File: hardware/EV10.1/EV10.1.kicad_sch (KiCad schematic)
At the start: 105 parts, among them J1 Conn_01x02_Socket, J10 Conn_01x08_Socket, J11 Conn_01x06_Female, J13 Conn_01x04_Female, J2 Conn_01x02_Female, J5 Conn_01x02_Socket, J7 Conn_01x04_Female, J8 Conn_01x06_Female, J9 USB_C_Receptacle, SW4 SW_Push, SW5 SW_Push, U1 STM32F405RGTx, U11 ESP32-S3-WROOM-1-N8R2, U13 BM14B(0.8)-24DS-0.4V(53), U2 BQ21040DBVR, U3 CH340C, U4 USBLC6-2P6, U5 STM32F030C8Tx, U6 WM8960CGEFL/RV, U7 TPS63060, Y1 Crystal_GND24

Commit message: Fix most warnings and errors in EV10.1
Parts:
- removed J9: USB_C_Receptacle, Connector_USB:USB_C_Receptacle_HRO_TYPE-C-31-M-12, symbol Connector:USB_C_Receptacle
- removed R2, R3: 5k1, Resistor_SMD:R_0402_1005Metric, symbol Device:R
- added R28, R29: 5k1, Resistor_SMD:R_0402_1005Metric, symbol Device:R
- added USB_C1: TYPE-C-31-M-12, Connector_USB:USB_C_Receptacle_HRO_TYPE-C-31-M-12, symbol jlcpcb:TYPE-C-31-M-12
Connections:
- net GND: now also U6.28 (AGND), R28.1, R29.1, USB_C1.0 (SH), USB_C1.A1 (GND), USB_C1.A12 (GND), USB_C1.B1 (GND), USB_C1.B12 (GND)
- net I2S_ADCDAT: now also U1.56 (PB4); no longer U1.52 (PC11)
- net I2S_DACDAT: now also U1.57 (PB5); no longer U1.53 (PC12)
- net KB_COL5: now also U1.53 (PC12); no longer U1.57 (PB5)
- net KB_ROW7: now also U1.52 (PC11); no longer U1.56 (PB4)
- net USB_D+: now also USB_C1.A6 (DP1), USB_C1.B6 (DP2)
- net USB_D-: now also USB_C1.A7 (DN1), USB_C1.B7 (DN2)
- net VBUS: now also USB_C1.A4 (VBUS), USB_C1.A9 (VBUS), USB_C1.B4 (VBUS), USB_C1.B9 (VBUS)
- new net: R29.2, USB_C1.B5 (CC2)
- new net: R28.2, USB_C1.A5 (CC1)
- no-connect marks 77 -> 67
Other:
- note added: "TEST POINTS"
- moved on the sheet: C32, R7, R8, U3, U4

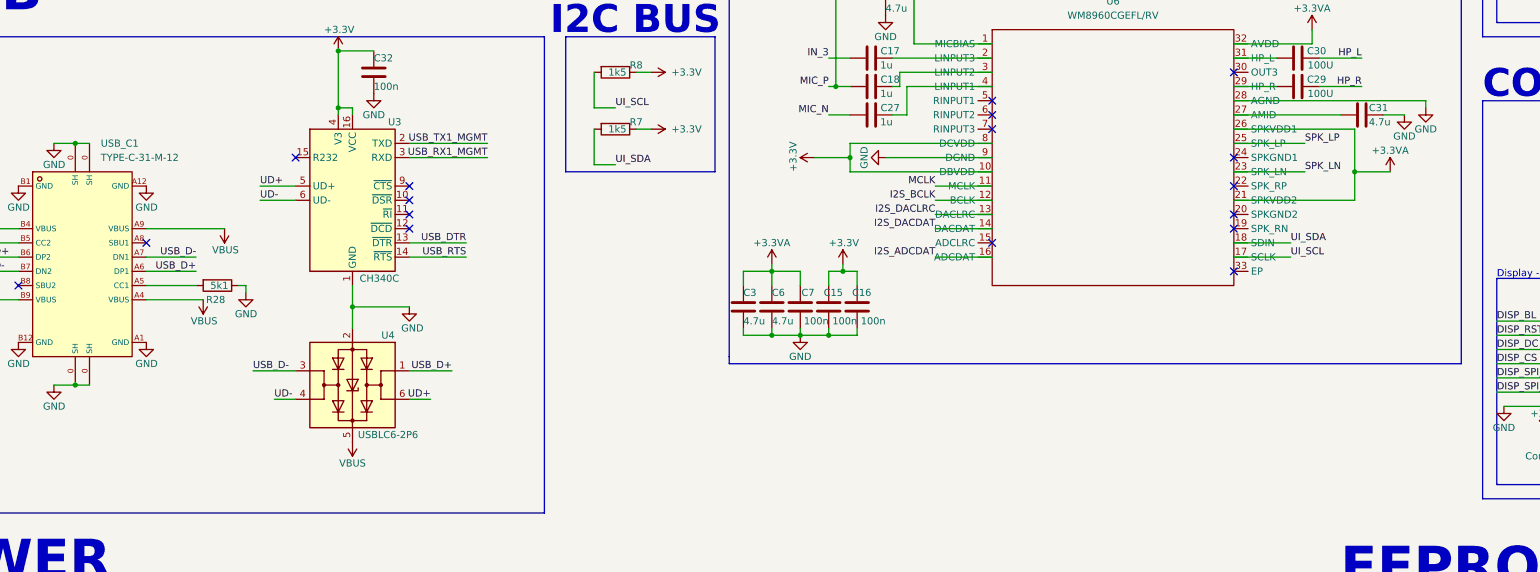
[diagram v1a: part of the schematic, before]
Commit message: Updated symbols and footprints to be jlcpcb specific
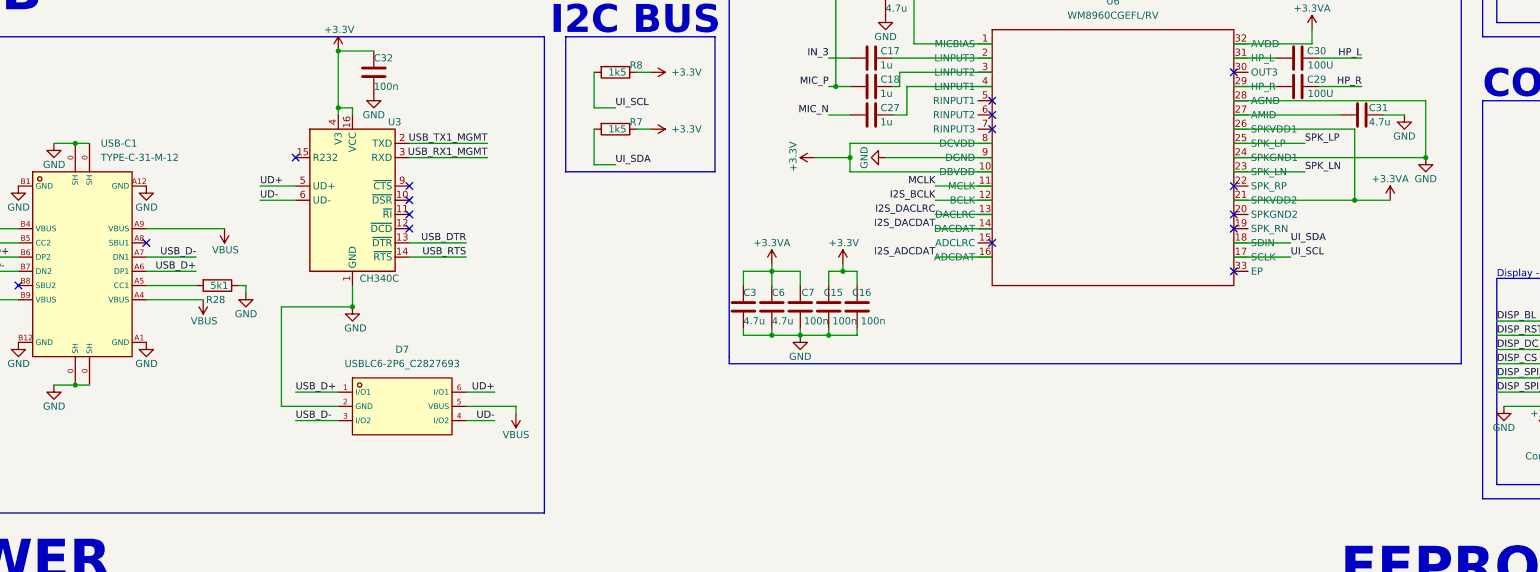
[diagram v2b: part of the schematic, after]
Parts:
- removed U4: USBLC6-2P6, Package_TO_SOT_SMD:SOT-666, symbol Power_Protection:USBLC6-2P6
- removed USB_C1: TYPE-C-31-M-12, Connector_USB:USB_C_Receptacle_HRO_TYPE-C-31-M-12, symbol jlcpcb:TYPE-C-31-M-12
- added D7: USBLC6-2P6_C2827693, jlc_pcb:SOT-666-6_L1.6-W1.2-P0.50-LS1.6-BL, symbol jlcpcb:USBLC6-2P6_C2827693
- added USB-C1: TYPE-C-31-M-12, footprint:USB-C_SMD-TYPE-C-31-M-12, symbol TYPE-C-31-M-12:TYPE-C-31-M-12
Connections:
- net GND: now also U6.24 (SPKGND1), D7.2 (GND), USB-C1.0 (SH), USB-C1.A1 (GND), USB-C1.A12 (GND), USB-C1.B1 (GND), USB-C1.B12 (GND)
- net UD+: now also D7.6 (I/O1)
- net UD-: now also D7.4 (I/O2)
- net USB_D+: now also D7.1 (I/O1), USB-C1.A6 (DP1), USB-C1.B6 (DP2)
- net USB_D-: now also D7.3 (I/O2), USB-C1.A7 (DN1), USB-C1.B7 (DN2)
- net VBUS: now also D7.5 (VBUS), USB-C1.A4 (VBUS), USB-C1.A9 (VBUS), USB-C1.B4 (VBUS), USB-C1.B9 (VBUS)
- net at R29.2: now also USB-C1.B5 (CC2)
- net at R28.2: now also USB-C1.A5 (CC1)
- no-connect marks 67 -> 66

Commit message: Update jlcpcb labels, and some rotations and positions
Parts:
- 120R1: JLCPCB# C127301 -> (none); LCSC Part # (none) -> C127301
- C10, C17, C18, C27, C9: JLCPCB# C52923 -> (none); LCSC Part # (none) -> C52923
- C11, C12, C13, C14, C15, C16, C24, C25, C26, C32, C34, C35, C36, C7: JLCPCB# C1525 -> (none); LCSC Part # (none) -> C1525
- C21, C22: JLCPCB# C12530 -> (none); LCSC Part # (none) -> C12530
- C23, C4: JLCPCB# C107115 -> (none); LCSC Part # (none) -> C107115
- C28, C3, C31, C6: JLCPCB# C23733 -> (none); LCSC Part # (none) -> C23733
- C29, C30: JLCPCB# C15008 -> (none); LCSC Part # (none) -> C15008
- C8: JLCPCB# C15195 -> (none); LCSC Part # (none) -> C15195
- CR1: JLCPCB Rotation Offset (none) -> 90; JLCPCB# C83836 -> (none); LCSC Part # (none) -> C83836
- D18, D3, D4, D5: JLCPCB Position Offset (none) -> 0.70,0.35; JLCPCB# C2874115 -> (none); LCSC Part # (none) -> C2874115
- D7: LCSC C2827693 -> (none); LCSC Part # (none) -> C2827693
- J1, J5: JLCPCB Rotation Offset (none) -> 180; LCSC Part # (none) -> C295747
- J10: LCSC Part # (none) -> C3029349
- J11, J8: JLCPCB# C265405 -> (none); LCSC Part # (none) -> C265405
- J13: JLCPCB Position Offset (none) -> 2.66,1.8; JLCPCB# C3029343 -> (none); LCSC Part # (none) -> C3029343
- J2: JLCPCB Rotation Offset (none) -> 180; JLCPCB# C295747 -> (none); LCSC Part # (none) -> C295747
- J7: JLCPCB Position Offset (none) -> 2.50,2.2; JLCPCB# C3029343 -> (none); LCSC Part # (none) -> C3029343
- R10, R32, R5: JLCPCB# C25900 -> (none); LCSC Part # (none) -> C25900
- R11, R12, R14, R15, R17, R18, R24, R25: JLCPCB# C25082 -> (none); LCSC Part # (none) -> C25082
- R13, R16, R23, R6: JLCPCB# C25087 -> (none); LCSC Part # (none) -> C25087
- R28, R29: JLCPCB# C25905 -> (none); LCSC Part # (none) -> C25905
- R4: JLCPCB# C25756 -> (none); LCSC Part # (none) -> C25756
- R41: JLCPCB# C17168 -> (none); LCSC Part # (none) -> C17168
- R7, R8: JLCPCB# C25867 -> (none); LCSC Part # (none) -> C25867
- R9: JLCPCB# C25879 -> (none); LCSC Part # (none) -> C25879
- SW4, SW5: JLCPCB# C266189 -> (none); LCSC Part # (none) -> C266189
- U1: JLCPCB# C15742 -> (none); LCSC Part # (none) -> C15742
- U11: JLCPCB# C3013944 -> (none); LCSC Part # (none) -> C3013944
- U3: JLCPCB# C84681 -> (none); LCSC Part # (none) -> C84681
- U5: JLCPCB# C80488 -> (none); LCSC Part # (none) -> C80488
- U6: JLCPCB# C18752 -> (none); LCSC Part # (none) -> C18752
- USB-C1: LCSC C165948 -> (none); LCSC Part # (none) -> C165948
- Y1: JLCPCB# C13738 -> (none); LCSC Part # (none) -> C13738

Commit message: All pcb components are orientated correctly in jlcpcb pick n place tool
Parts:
- CR1: JLCPCB Rotation Offset 90 -> -90
- J13: JLCPCB Position Offset 2.66,1.8 -> 2.59,1.73
- J7: JLCPCB Position Offset 2.50,2.2 -> 2.59,1.73
- U2: JLCPCB Rotation Offset (none) -> 180
- U7: JLCPCB Rotation Offset (none) -> -90
- USB-C1: JLCPCB Position Offset (none) -> 0, 1.0
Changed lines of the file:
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@@
 			)
 		)
-		(property "JLCPCB Rotation Offset" "90"
+		(property "JLCPCB Rotation Offset" "-90"
 			(at 292.1 303.53 0)
 			(effects
@@
 			)
 		)
+		(property "JLCPCB Rotation Offset" "180"
+			(at 58.42 328.93 0)
+			(effects
+				(font
+					(size 1.27 1.27)
+				)
+				(hide yes)
+			)
+		)
 		(pin "1"
 		)
@@
 			)
 		)
-		(property "JLCPCB Position Offset" "2.50,2.2"
+		(property "JLCPCB Position Offset" "2.59,1.73"
 			(at 383.54 247.65 0)
 			(effects
@@
 			)
 		)
+		(property "JLCPCB Rotation Offset" "-90"
+			(at 156.21 327.66 0)
+			(effects
+				(font
+					(size 1.27 1.27)
+				)
+				(hide yes)
+			)
+		)
 		(pin "1"
 		)
@@
 			)
 		)
+		(property "JLCPCB Position Offset" "0, 1.0"
+			(at 58.42 236.22 0)
+			(effects
+				(font
+					(size 1.27 1.27)
+				)
+				(hide yes)
+			)
+		)
 		(pin "A9"
 		)
@@
 			)
 		)
-		(property "JLCPCB Position Offset" "2.66,1.8"
+		(property "JLCPCB Position Offset" "2.59,1.73"
 			(at 403.86 219.71 0)
 			(effects

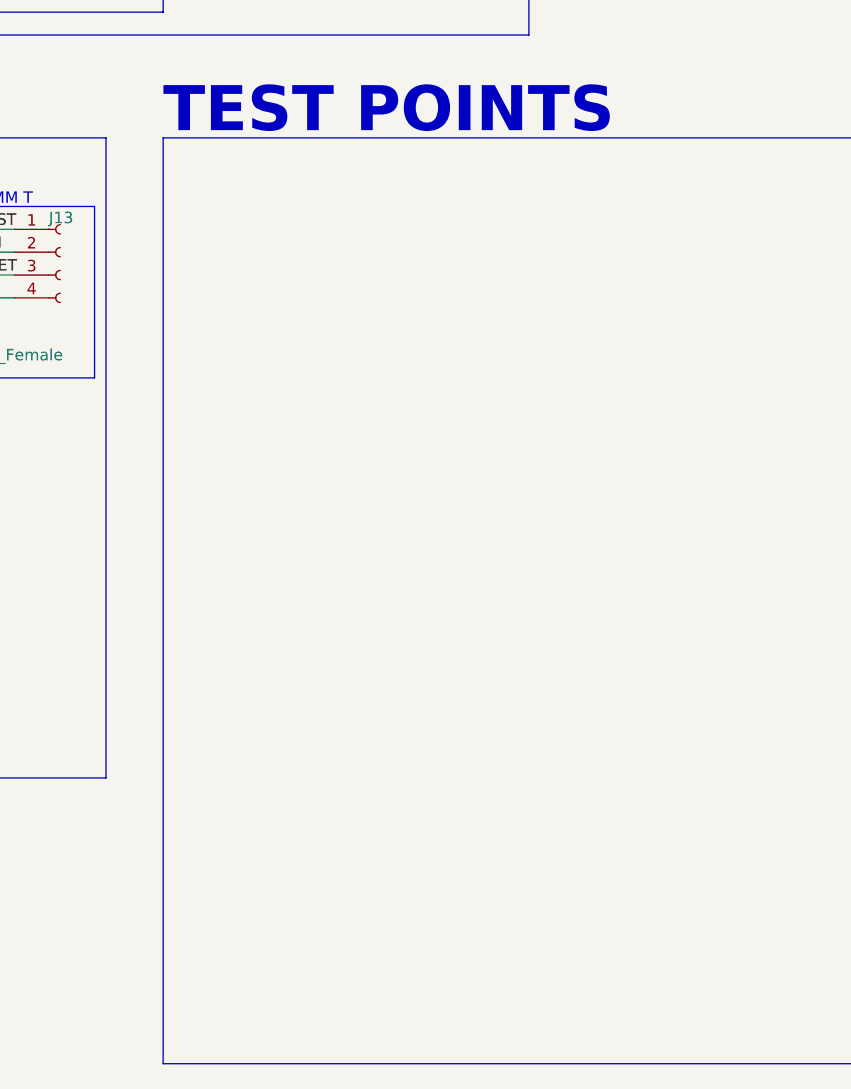
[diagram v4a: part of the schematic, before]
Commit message: Adding test points
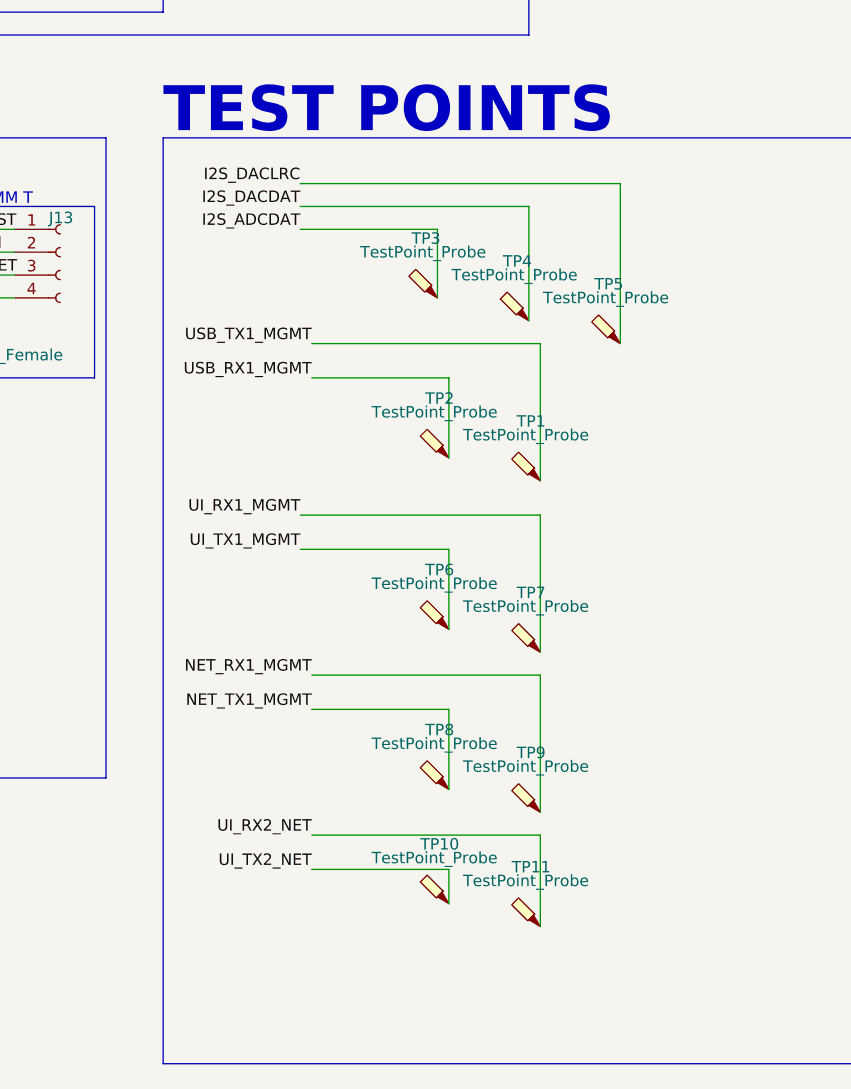
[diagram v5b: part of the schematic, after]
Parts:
- added TP1, TP10, TP11, TP2, TP3, TP4, TP5, TP6, TP7, TP8, TP9: TestPoint_Probe, TestPoint:TestPoint_Keystone_5000-5004_Miniature, symbol Connector:TestPoint_Probe
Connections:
- net I2S_ADCDAT: now also TP3.1
- net I2S_DACDAT: now also TP4.1
- net I2S_DACLRC: now also TP5.1
- net NET_RX1_MGMT: now also TP9.1
- net NET_TX1_MGMT: now also TP8.1
- net UI_RX1_MGMT: now also TP7.1
- net UI_RX2_NET: now also TP11.1
- net UI_TX1_MGMT: now also TP6.1
- net UI_TX2_NET: now also TP10.1
- net USB_RX1_MGMT: now also TP2.1
- net USB_TX1_MGMT: now also TP1.1

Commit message: EV10.1 is ready for review
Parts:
- added TP12: P_GND, TestPoint:TestPoint_Keystone_5000-5004_Miniature, symbol Connector:TestPoint_Probe
- TP1: value TestPoint_Probe -> P_USB_TX_MGMT
- TP10, TP11: value TestPoint_Probe -> P_UI_RX_NET
- TP2: value TestPoint_Probe -> P_USB_RX_MGMT
- TP3: value TestPoint_Probe -> P_I2S_ADCDAT
- TP4: value TestPoint_Probe -> P_I2S_DACDAT
- TP5: value TestPoint_Probe -> P_I2S_DACLRC
- TP6: value TestPoint_Probe -> P_UI_TX_MGMT
- TP7: value TestPoint_Probe -> P_UI_RX_MGMT
- TP8: value TestPoint_Probe -> P_NET_TX_MGMT
- TP9: value TestPoint_Probe -> P_NET_RX_MGMT
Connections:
- net +3.3V: now also U13.2
- net GND: now also TP12.1; no longer U13.2, U13.3
- net KB_MIC: now also U13.3

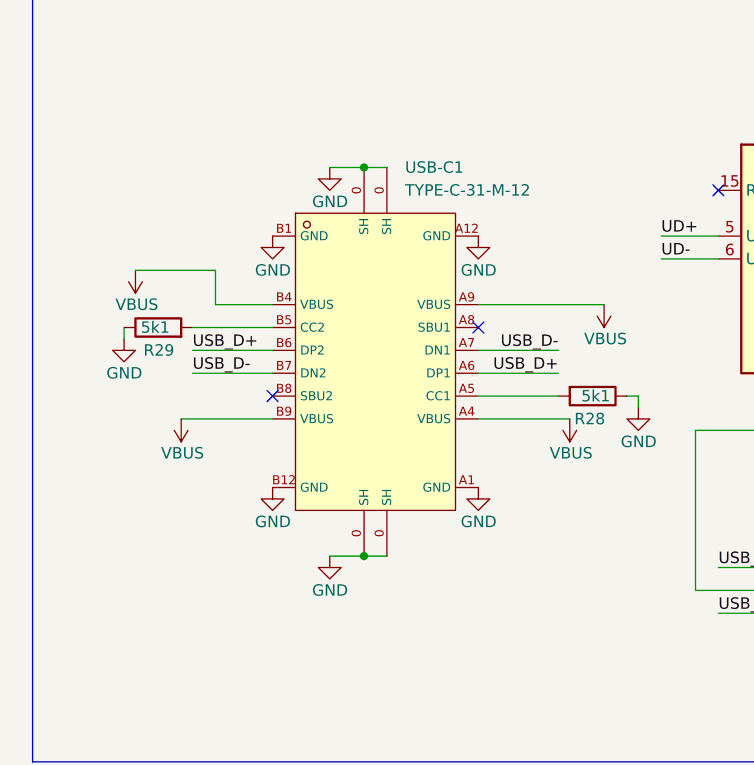
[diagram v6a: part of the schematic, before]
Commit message: Fixed mistake that grounded the usb-c shield
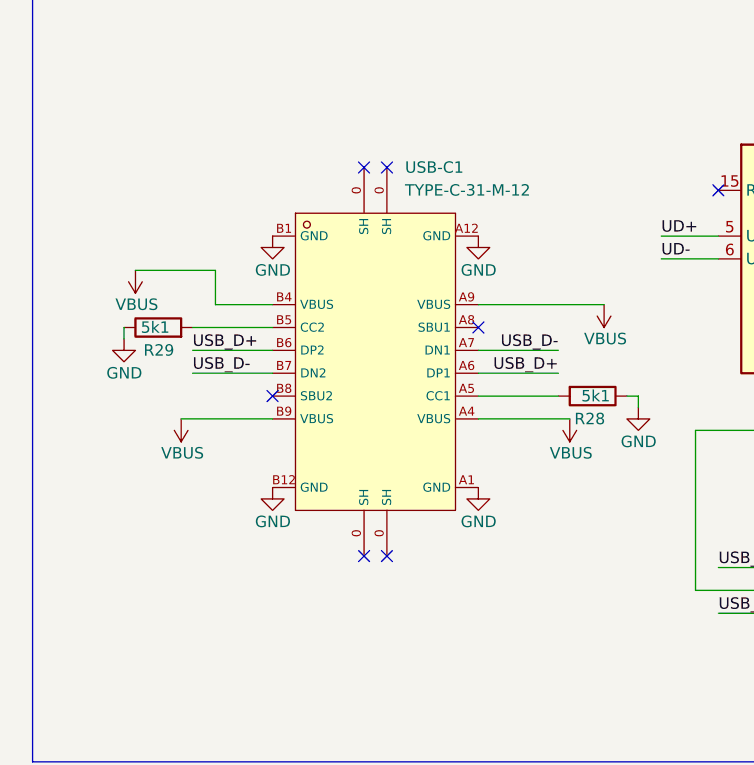
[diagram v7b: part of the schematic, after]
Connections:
- net GND: no longer USB-C1.0 (SH)
- no-connect marks 66 -> 70
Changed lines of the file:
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@@
 	)
 	(junction
-		(at 57.15 214.63)
-		(diameter 0)
-		(color 0 0 0 0)
-	)
-	(junction
 		(at 327.66 78.74)
 		(diameter 0)
@@
 	)
 	(junction
-		(at 57.15 257.81)
-		(diameter 0)
-		(color 0 0 0 0)
-	)
-	(junction
 		(at 359.41 78.74)
 		(diameter 0)
@@
 	)
 	(no_connect
+		(at 57.15 214.63)
+	)
+	(no_connect
 		(at 214.63 113.03)
 	)
@@
 	)
 	(no_connect
+		(at 57.15 257.81)
+	)
+	(no_connect
 		(at 214.63 133.35)
 	)
@@
 	)
 	(no_connect
+		(at 59.69 257.81)
+	)
+	(no_connect
+		(at 59.69 214.63)
+	)
+	(no_connect
 		(at 81.28 129.54)
 	)
@@
 	(wire
 		(pts
-			(xy 53.34 257.81) (xy 57.15 257.81)
-		)
-		(stroke
-			(width 0)
-			(type default)
-		)
-	)
-	(wire
-		(pts
 			(xy 132.08 163.83) (xy 130.81 163.83)
 		)
@@
 		)
 	)
-	(wire
-		(pts
-			(xy 53.34 214.63) (xy 57.15 214.63)
-		)
-		(stroke
-			(width 0)
-			(type default)
-		)
-	)
 	(polyline
 		(pts
@@
 	(wire
 		(pts
-			(xy 57.15 214.63) (xy 59.69 214.63)
-		)
-		(stroke
-			(width 0)
-			(type default)
-		)
-	)
-	(wire
-		(pts
 			(xy 93.98 243.84) (xy 106.68 243.84)
 		)
@@
 	(wire
 		(pts
-			(xy 57.15 257.81) (xy 59.69 257.81)
-		)
-		(stroke
-			(width 0)
-			(type default)
-		)
-	)
-	(wire
-		(pts
 			(xy 99.06 86.36) (xy 99.06 85.09)
 		)
@@
 	)
 	(symbol
-		(lib_name "GND_20")
-		(lib_id "power:GND")
-		(at 53.34 214.63 0)
-		(unit 1)
-		(exclude_from_sim no)
-		(in_bom yes)
-		(on_board yes)
-		(dnp no)
-		(property "Reference" "#PWR019"
-			(at 53.34 220.98 0)
-			(effects
-				(font
-					(size 1.27 1.27)
-				)
-				(hide yes)
-			)
-		)
-		(property "Value" "GND"
-			(at 55.372 218.44 0)
-			(effects
-				(font
-					(size 1.27 1.27)
-				)
-				(justify right)
-			)
-		)
-		(property "Footprint" ""
-			(at 53.34 214.63 0)
-			(effects
-				(font
-					(size 1.27 1.27)
-				)
-				(hide yes)
-			)
-		)
-		(property "Datasheet" ""
-			(at 53.34 214.63 0)
-			(effects
-				(font
-					(size 1.27 1.27)
-				)
-				(hide yes)
-			)
-		)
-		(property "Description" ""
-			(at 53.34 214.63 0)
-			(effects
-				(font
-					(size 1.27 1.27)
-				)
-				(hide yes)
-			)
-		)
-		(pin "1"
-		)
-		(instances
-			(project "EV10.1"
-				(path "/bd865368-262b-4f76-b7a6-1673c2cb0f8c"
-					(reference "#PWR019")
-					(unit 1)
-				)
-			)
-		)
-	)
-	(symbol
 		(lib_id "Device:R")
 		(at 139.7 109.22 270)
@@
 					(unit 1)
 				)
-			)
-		)
-	)
-	(symbol
-		(lib_name "GND_17")
-		(lib_id "power:GND")
-		(at 53.34 257.81 0)
-		(unit 1)
-		(exclude_from_sim no)
-		(in_bom yes)
-		(on_board yes)
-		(dnp no)
-		(property "Reference" "#PWR020"
-			(at 53.34 264.16 0)
-			(effects
-				(font
-					(size 1.27 1.27)
-				)
-				(hide yes)
-			)
-		)
-		(property "Value" "GND"
-			(at 55.372 261.62 0)
-			(effects
-				(font
-					(size 1.27 1.27)
-				)
-				(justify right)
-			)
-		)
-		(property "Footprint" ""
-			(at 53.34 257.81 0)
-			(effects
-				(font
-					(size 1.27 1.27)
-				)
-				(hide yes)
-			)
-		)
-		(property "Datasheet" ""
-			(at 53.34 257.81 0)
-			(effects
-				(font
-					(size 1.27 1.27)
-				)
-				(hide yes)
-			)
-		)
-		(property "Description" ""
-			(at 53.34 257.81 0)
-			(effects
-				(font
-					(size 1.27 1.27)
-				)
-				(hide yes)
-			)
-		)
-		(pin "1"
-		)
-		(instances
-			(project "EV10.1"
-				(path "/bd865368-262b-4f76-b7a6-1673c2cb0f8c"
-					(reference "#PWR020")
-					(unit 1)
-				)
